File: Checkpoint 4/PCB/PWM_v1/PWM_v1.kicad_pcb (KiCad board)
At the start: 2 copper layers, 90 x 45 mm, 31 parts, among them J1 Conn_01x02, J2 Conn_01x02, U1 LM7809_TO220, U2 LM393, U3 TL062

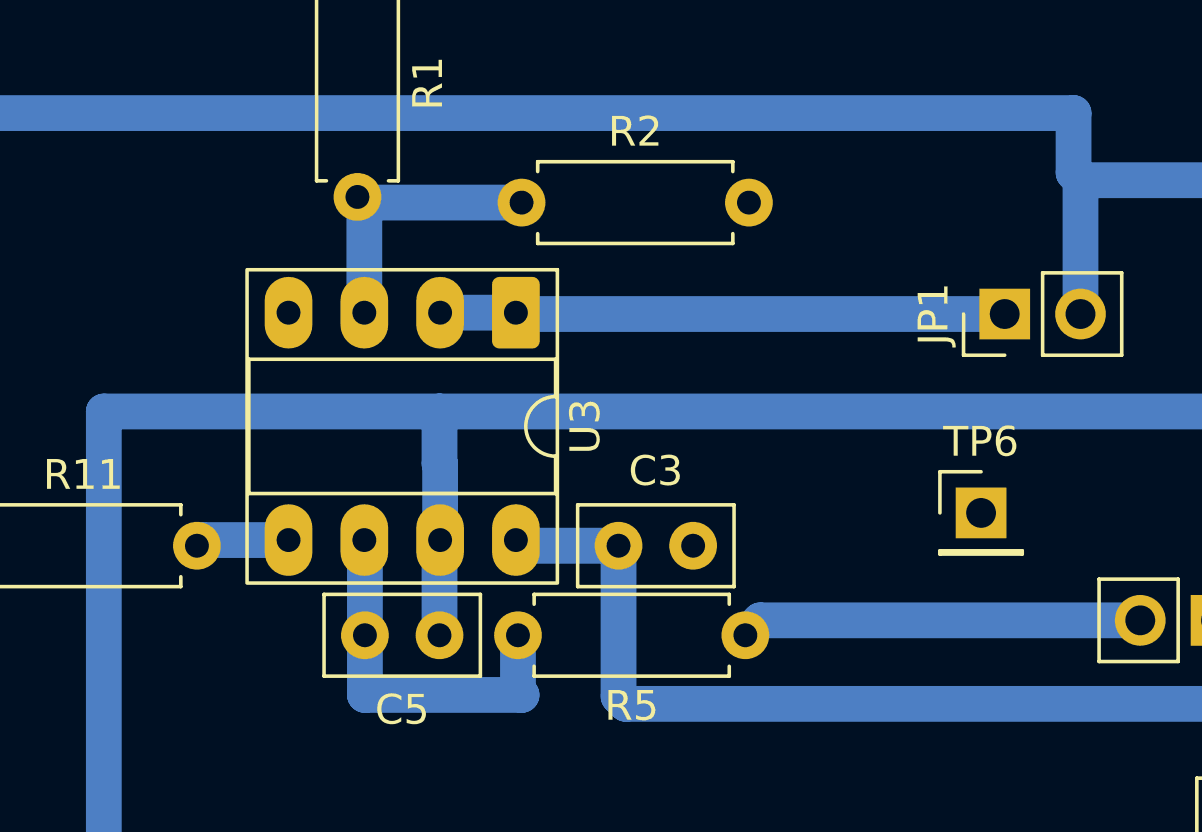
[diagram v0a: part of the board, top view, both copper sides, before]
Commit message: Cambié el TL062 por el TL072
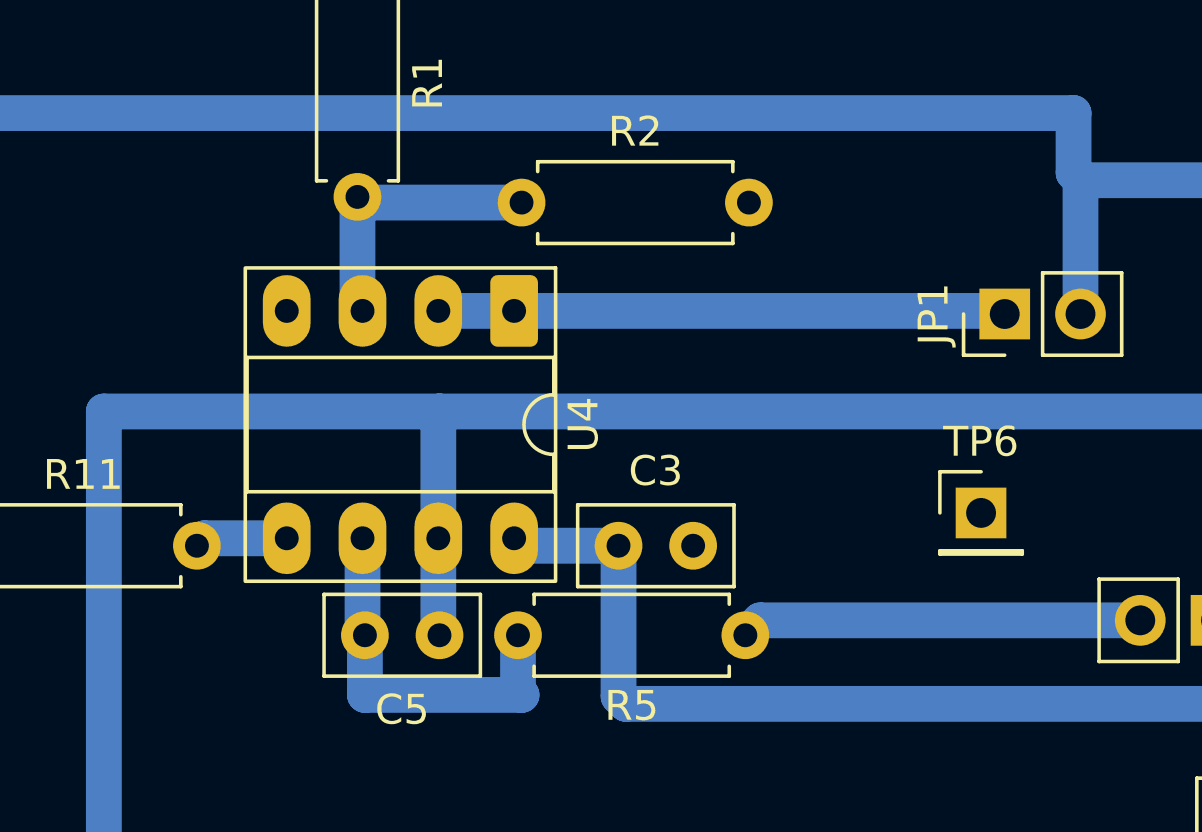
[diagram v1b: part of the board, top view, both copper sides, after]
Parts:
- removed U3: TL062, Package_DIP:DIP-8_W7.62mm_Socket_LongPads
- added U4: TL072, Package_DIP:DIP-8_W7.62mm_Socket_LongPads, F.Cu at (111.8, 109.6)
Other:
- board text added: "Nota para el próximo PCB: Priorizar las pistas de señal. Hacerlas lo más cortas posibles. Las pistas de alimentación importan menos"

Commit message: cambié un poco la simulación
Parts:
- C1, C3, C4: value C -> 0.1u
- C2: value C -> 0.33u
- R1, R2, Rf1: value 510k -> 560k
- R7, R8: value R -> 10k
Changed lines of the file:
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@@
 			)
 		)
-		(property "Value" "510k"
+		(property "Value" "560k"
 			(at 3.81 2.37 0)
 			(layer "F.Fab")
@@
 			)
 		)
-		(property "Value" "C"
+		(property "Value" "0.1u"
 			(at 1.25 2.5 0)
 			(layer "F.Fab")
@@
 			)
 		)
-		(property "Value" "510k"
+		(property "Value" "560k"
 			(at 3.81 2.37 0)
 			(layer "F.Fab")
@@
 			)
 		)
-		(property "Value" "C"
+		(property "Value" "0.1u"
 			(at 1.25 2.5 0)
 			(layer "F.Fab")
@@
 			)
 		)
-		(property "Value" "C"
+		(property "Value" "0.1u"
 			(at 4.75 0 0)
 			(layer "F.Fab")
@@
 			)
 		)
-		(property "Value" "C"
+		(property "Value" "0.33u"
 			(at 1.25 2.5 0)
 			(layer "F.Fab")
@@
 			)
 		)
-		(property "Value" "R"
+		(property "Value" "10k"
 			(at 3.714327 4.25 90)
 			(layer "F.Fab")
@@
 			)
 		)
-		(property "Value" "R"
+		(property "Value" "10k"
 			(at 3.81 2.37 0)
 			(layer "F.Fab")
@@
 			)
 		)
-		(property "Value" "510k"
+		(property "Value" "560k"
 			(at 3.81 2.37 90)
 			(layer "F.Fab")
@@
 	)
 	(segment
-		(start 111.75 109.63)
-		(end 109.21 109.63)
+		(start 106.5 105.81)
+		(end 106.5 109.46)
 		(width 1.2)
 		(layer "B.Cu")
-		(net "Net-(JP1-A)")
+		(net "Net-(U4A-+)")
 	)
 	(segment
-		(start 111.75 109.63)
-		(end 128.087998 109.63)
+		(start 106.73 106.04)
+		(end 106.5 105.81)
 		(width 1.2)
 		(layer "B.Cu")
-		(net "Net-(JP1-A)")
+		(net "Net-(U4A-+)")
 	)
 	(segment
-		(start 128.087998 109.63)
-		(end 128.192253 109.734255)
+		(start 106.5 109.46)
+		(end 106.67 109.63)
 		(width 1.2)
 		(layer "B.Cu")
-		(net "Net-(JP1-A)")
+		(net "Net-(U4A-+)")
 	)
 	(segment
-		(start 104.13 117.25)
-		(end 101.37 117.25)
+		(start 106.69 106)
+		(end 106.5 105.81)
 		(width 1.2)
 		(layer "B.Cu")
-		(net "/Vref_opamp")
+		(net "Net-(U4A-+)")
 	)
 	(segment
-		(start 101.37 117.25)
-		(end 101.12 117.5)
+		(start 112 106)
+		(end 106.69 106)
 		(width 1.2)
 		(layer "B.Cu")
-		(net "/Vref_opamp")
+		(net "Net-(U4A-+)")
 	)
 	(segment
@@
 	)
 	(segment
-		(start 146.25 105.25)
-		(end 146.58 105.58)
+		(start 106.75 120.5)
+		(end 106.75 122.5)
 		(width 1.2)
 		(layer "B.Cu")
-		(net "/Vref")
+		(net "Net-(U4B--)")
 	)
 	(segment
-		(start 130.75 105.25)
-		(end 146.25 105.25)
+		(start 106.67 117.25)
+		(end 106.67 120.42)
 		(width 1.2)
 		(layer "B.Cu")
-		(net "/Vref")
+		(net "Net-(U4B--)")
 	)
 	(segment
-		(start 93.5 103)
-		(end 130.5 103)
+		(start 106.67 120.42)
+		(end 106.75 120.5)
 		(width 1.2)
 		(layer "B.Cu")
-		(net "/Vref")
+		(net "Net-(U4B--)")
 	)
 	(segment
-		(start 130.5 103)
-		(end 130.5 105)
+		(start 106.75 122.5)
+		(end 112 122.5)
 		(width 1.2)
 		(layer "B.Cu")
-		(net "/Vref")
+		(net "Net-(U4B--)")
 	)
 	(segment
-		(start 130.732253 109.734255)
-		(end 130.732253 105.267747)
+		(start 111.88 122.38)
+		(end 111.88 120.5)
 		(width 1.2)
 		(layer "B.Cu")
-		(net "/Vref")
+		(net "Net-(U4B--)")
 	)
 	(segment
-		(start 130.5 105)
-		(end 130.75 105.25)
+		(start 112 122.5)
+		(end 111.88 122.38)
 		(width 1.2)
 		(layer "B.Cu")
-		(net "/Vref")
+		(net "Net-(U4B--)")
 	)
 	(segment
-		(start 93.5 117.5)
-		(end 93.5 103)
+		(start 111.75 109.63)
+		(end 109.21 109.63)
 		(width 1.2)
 		(layer "B.Cu")
-		(net "/Vref")
+		(net "Net-(JP1-A)")
 	)
 	(segment
-		(start 130.732253 105.267747)
-		(end 130.75 105.25)
+		(start 111.75 109.63)
+		(end 128.087998 109.63)
 		(width 1.2)
 		(layer "B.Cu")
-		(net "/Vref")
+		(net "Net-(JP1-A)")
 	)
 	(segment
-		(start 146.58 105.58)
-		(end 146.58 117.19)
+		(start 128.087998 109.63)
+		(end 128.192253 109.734255)
 		(width 1.2)
 		(layer "B.Cu")
-		(net "/Vref")
+		(net "Net-(JP1-A)")
 	)
 	(segment
-		(start 141.44 124.75)
-		(end 141.5 124.81)
+		(start 104.13 117.25)
+		(end 101.37 117.25)
 		(width 1.2)
 		(layer "B.Cu")
-		(net "/PWM_ref")
+		(net "/Vref_opamp")
 	)
 	(segment
-		(start 136 124.75)
-		(end 141.44 124.75)
+		(start 101.37 117.25)
+		(end 101.12 117.5)
 		(width 1.2)
 		(layer "B.Cu")
-		(net "/PWM_ref")
+		(net "/Vref_opamp")
 	)
 	(segment
-		(start 131.765 132.25)
-		(end 135.88 132.25)
+		(start 146.25 105.25)
+		(end 146.58 105.58)
 		(width 1.2)
 		(layer "B.Cu")
-		(net "Net-(JP5-B)")
+		(net "/Vref")
 	)
 	(segment
-		(start 135.88 132.25)
-		(end 136 132.37)
+		(start 130.75 105.25)
+		(end 146.25 105.25)
 		(width 1.2)
 		(layer "B.Cu")
-		(net "Net-(JP5-B)")
+		(net "/Vref")
 	)
 	(segment
-		(start 106.75 120.5)
-		(end 106.75 122.5)
+		(start 93.5 103)
+		(end 130.5 103)
 		(width 1.2)
 		(layer "B.Cu")
-		(net "Net-(U4B--)")
+		(net "/Vref")
 	)
 	(segment
-		(start 106.67 117.25)
-		(end 106.67 120.42)
+		(start 130.5 103)
+		(end 130.5 105)
 		(width 1.2)
 		(layer "B.Cu")
-		(net "Net-(U4B--)")
+		(net "/Vref")
 	)
 	(segment
-		(start 106.67 120.42)
-		(end 106.75 120.5)
+		(start 130.732253 109.734255)
+		(end 130.732253 105.267747)
 		(width 1.2)
 		(layer "B.Cu")
-		(net "Net-(U4B--)")
+		(net "/Vref")
 	)
 	(segment
-		(start 106.75 122.5)
-		(end 112 122.5)
+		(start 130.5 105)
+		(end 130.75 105.25)
 		(width 1.2)
 		(layer "B.Cu")
-		(net "Net-(U4B--)")
+		(net "/Vref")
 	)
 	(segment
-		(start 111.88 122.38)
-		(end 111.88 120.5)
+		(start 93.5 117.5)
+		(end 93.5 103)
 		(width 1.2)
 		(layer "B.Cu")
-		(net "Net-(U4B--)")
+		(net "/Vref")
 	)
 	(segment
-		(start 112 122.5)
-		(end 111.88 122.38)
+		(start 130.732253 105.267747)
+		(end 130.75 105.25)
 		(width 1.2)
 		(layer "B.Cu")
-		(net "Net-(U4B--)")
+		(net "/Vref")
 	)
 	(segment
-		(start 106.5 105.81)
-		(end 106.5 109.46)
+		(start 146.58 105.58)
+		(end 146.58 117.19)
 		(width 1.2)
 		(layer "B.Cu")
-		(net "Net-(U4A-+)")
+		(net "/Vref")
 	)
 	(segment
-		(start 106.73 106.04)
-		(end 106.5 105.81)
+		(start 141.44 124.75)
+		(end 141.5 124.81)
 		(width 1.2)
 		(layer "B.Cu")
-		(net "Net-(U4A-+)")
+		(net "/PWM_ref")
 	)
 	(segment
-		(start 106.5 109.46)
-		(end 106.67 109.63)
+		(start 136 124.75)
+		(end 141.44 124.75)
 		(width 1.2)
 		(layer "B.Cu")
-		(net "Net-(U4A-+)")
+		(net "/PWM_ref")
 	)
 	(segment
-		(start 106.69 106)
-		(end 106.5 105.81)
+		(start 131.765 132.25)
+		(end 135.88 132.25)
 		(width 1.2)
 		(layer "B.Cu")
-		(net "Net-(U4A-+)")
+		(net "Net-(JP5-B)")
 	)
 	(segment
-		(start 112 106)
-		(end 106.69 106)
+		(start 135.88 132.25)
+		(end 136 132.37)
 		(width 1.2)
 		(layer "B.Cu")
-		(net "Net-(U4A-+)")
+		(net "Net-(JP5-B)")
 	)
 	(zone
